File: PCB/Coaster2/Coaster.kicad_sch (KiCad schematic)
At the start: 1028 parts, among them J1 Conn_01x03, J2 Conn_01x03

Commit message: Improved for new KiCAD - needs more work on track nets
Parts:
- removed C212, C213, C214, C215, C216, C217, C218, C219, C220, C221, C222, C223, C224, C225, C226, C227, C228, C229, C230, C231, C232, C233, C234, C235, C236, C237, C238, C239, C240, C241, C242, C243, C244, C245, C246, C247, C248, C249, C250, C251, C252, C253, C254, C255, C256, C257, C258, C259, C260, C261, C262, C263, C264, C265, C266, C267, C268, C269, C270, C271, C272, C273, C274, C275, C276, C277, C278, C279, C280, C281, C282, C283, C284, C285, C286, C287, C288, C289, C290, C291, C292, C293, C294, C295, C296, C297, C298, C299, C300, C301, C302, C303, C304, C305, C306, C307, C308, C309, C310, C311, C312, C313, C314, C315, C316, C317, C318, C319, C320, C321, C322, C323, C324, C325, C326, C327, C328, C329, C330, C331, C332, C333, C334, C335, C336, C337, C338, C339, C340, C341, C342, C343, C344, C345, C346, C347, C348, C349, C350, C351, C352, C353, C354, C355, C356, C357, C358, C359, C360, C361, C362, C363, C364, C365, C366, C367, C368, C369, C370, C371, C372, C373, C374, C375, C376, C377, C378, C379, C380, C381, C382, C383, C384, C385, C386, C387, C388, C389, C390, C391, C392, C393, C394, C395, C396, C397, C398, C399, C400, C401, C402, C403, C404, C405, C406, C407, C408, C409, C410, C411, C412, C413, C414, C415, C416, C417, C418, C419, C420, C421, C422, C423, C424, C425, C426, C427, C428, C429, C430, C431, C432, C433, C434, C435, C436, C437, C438, C439, C440, C441, C442, C443, C444, C445, C446, C447, C448, C449, C450, C451, C452, C453, C454, C455, C456, C457, C458, C459, C460, C461, C462, C463, C464, C465, C466, C467, C468, C469, C470, C471, C472, C473, C474, C475, C476, C477, C478, C479, C480, C481, C482, C483, C484, C485, C486, C487, C488, C489, C490, C491, C492, C493, C494, C495, C496, C497, C498, C499, C500, C501, C502, C503, C504, C505, C506, C507: 100nF, RevK:C_0402, symbol Device:C
- removed D212, D213, D214, D215, D216, D217, D218, D219, D220, D221, D222, D223, D224, D225, D226, D227, D228, D229, D230, D231, D232, D233, D234, D235, D236, D237, D238, D239, D240, D241, D242, D243, D244, D245, D246, D247, D248, D249, D250, D251, D252, D253, D254, D255, D256, D257, D258, D259, D260, D261, D262, D263, D264, D265, D266, D267, D268, D269, D270, D271, D272, D273, D274, D275, D276, D277, D278, D279, D280, D281, D282, D283, D284, D285, D286, D287, D288, D289, D290, D291, D292, D293, D294, D295, D296, D297, D298, D299, D300, D301, D302, D303, D304, D305, D306, D307, D308, D309, D310, D311, D312, D313, D314, D315, D316, D317, D318, D319, D320, D321, D322, D323, D324, D325, D326, D327, D328, D329, D330, D331, D332, D333, D334, D335, D336, D337, D338, D339, D340, D341, D342, D343, D344, D345, D346, D347, D348, D349, D350, D351, D352, D353, D354, D355, D356, D357, D358, D359, D360, D361, D362, D363, D364, D365, D366, D367, D368, D369, D370, D371, D372, D373, D374, D375, D376, D377, D378, D379, D380, D381, D382, D383, D384, D385, D386, D387, D388, D389, D390, D391, D392, D393, D394, D395, D396, D397, D398, D399, D400, D401, D402, D403, D404, D405, D406, D407, D408, D409, D410, D411, D412, D413, D414, D415, D416, D417, D418, D419, D420, D421, D422, D423, D424, D425, D426, D427, D428, D429, D430, D431, D432, D433, D434, D435, D436, D437, D438, D439, D440, D441, D442, D443, D444, D445, D446, D447, D448, D449, D450, D451, D452, D453, D454, D455, D456, D457, D458, D459, D460, D461, D462, D463, D464, D465, D466, D467, D468, D469, D470, D471, D472, D473, D474, D475, D476, D477, D478, D479, D480, D481, D482, D483, D484, D485, D486, D487, D488, D489, D490, D491, D492, D493, D494, D495, D496, D497, D498, D499, D500, D501, D502, D503, D504, D505, D506, D507: XL-1010RGBC-WS2812B, RevK:SMD1010, symbol RevK:WS2812B-1mm
- removed FID5, FID6: Fiducial, RevK:Hole-Tooling, symbol Mechanical:Fiducial
- removed J1, J2: Conn_01x03, RevK:3-PADS, symbol Connector_Generic:Conn_01x03
- removed Z5, Z6: Hidden, RevK:PCB-Join1, symbol RevK:Hidden
- FID4: footprint Fiducial:Fiducial_1mm_Mask2mm -> RevK:Hole-Tooling
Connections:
- net GND: no longer C208.2, C209.2, C210.2, C211.2, D208.3 (-), D209.3 (-), D210.3 (-), D211.3 (-)
- new net: C208.2, C209.2, C210.2, C211.2, D208.3 (-), D209.3 (-), D210.3 (-), D211.3 (-)
- no-connect marks 0 -> 1
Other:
- moved on the sheet: C1, C10, C100, C101, C102, C103, C104, C105, C106, C107, C108, C109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

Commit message: 199 LEDs
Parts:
- removed C200, C201, C202, C203, C204, C205, C206, C207, C208, C209, C210, C211: 100nF, RevK:C_0402, symbol Device:C
- removed D200, D201, D202, D203, D204, D205, D206, D207, D208, D209, D210, D211: XL-1010RGBC-WS2812B, RevK:SMD1010, symbol RevK:WS2812B-1mm
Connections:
- net GND: no longer C198.2, C199.2, D198.3 (-), D199.3 (-)
- new net: C198.2, C199.2, D198.3 (-), D199.3 (-)
- no-connect marks 1 -> 0

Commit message: Connection
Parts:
- added TP1: GND, RevK:Round, symbol Connector:TestPoint
- added TP2: DIN, RevK:Round, symbol Connector:TestPoint
- added TP3: PWR, RevK:Round, symbol Connector:TestPoint
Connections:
- net GND: now also C198.2, C199.2, D198.3 (-), D199.3 (-), TP1.1
- net VCC: now also TP3.1
- net at D1.4 (I): now also TP2.1

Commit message: Tracked
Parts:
- removed C103, C108, C109, C110, C111, C113, C114, C115, C116, C117, C118, C119, C120, C121, C122, C123, C124, C125, C126, C127, C128, C129, C130, C131, C132, C133, C134, C135, C136, C137, C138, C139, C140, C141, C142, C143, C144, C145, C146, C147, C148, C149, C150, C151, C152, C153, C154, C155, C156, C157, C158, C159, C160, C161, C162, C163, C164, C165, C166, C167, C168, C169, C170, C171, C172, C173, C174, C175, C176, C177, C178, C179, C180, C181, C182, C183, C184, C185, C186, C187, C188, C189, C190, C191, C192, C193, C194, C195, C196, C197, C198, C199: 100nF, RevK:C_0402, symbol Device:C
- removed D101, D102, D103, D104, D105, D106, D107, D108, D109, D110, D111, D112, D113, D114, D115, D116, D117, D118, D119, D120, D121, D122, D123, D124, D125, D126, D127, D128, D129, D130, D131, D132, D133, D134, D135, D136, D137, D138, D139, D140, D141, D142, D143, D144, D145, D146, D147, D148, D149, D150, D151, D152, D153, D154, D155, D156, D157, D158, D159, D160, D161, D162, D163, D164, D165, D166, D167, D168, D169, D170, D171, D172, D173, D174, D175, D176, D177, D178, D179, D180, D181, D182, D183, D184, D185, D186, D187, D188, D189, D190, D191, D192, D193, D194, D195, D196, D197, D198, D199: XL-1010RGBC-WS2812B, RevK:SMD1010, symbol RevK:WS2812B-1mm
- removed TP1: GND, RevK:Round, symbol Connector:TestPoint
- removed TP2: DIN, RevK:Round, symbol Connector:TestPoint
- removed TP3: PWR, RevK:Round, symbol Connector:TestPoint
- removed Z1, Z2, Z3, Z4: Hidden, RevK:PCB-Join1, symbol RevK:Hidden
- added C103: 220uF Tant, RevK:CP_EIA-3528-21_Kemet-B, symbol Device:C_Polarized
- added C109: 10uF 35V, RevK:C_0603_, symbol RevK:Hidden
- added C110: 10uF 6.3V, RevK:C_0603_, symbol RevK:Hidden
- added C111: 100nF, RevK:C_0603_, symbol RevK:Hidden
- added FID5: Fiducial, RevK:Hole-Tooling, symbol Mechanical:Fiducial
- added FID6: Fiducial, Fiducial:Fiducial_1mm_Mask2mm, symbol Mechanical:Fiducial
- added J1: Reset, RevK:AA-Pad, symbol Connector_Generic:Conn_01x02
- added J3: USB-C-Socket-H, RevK:USB-C-Socket-H, symbol RevK:USB-C-Socket-H
- added J4: TC2030-USB-NL-DS, RevK:Tag-Connect_TC2030-IDC-NL_2x03_P1.27mm_Vertical, symbol RevK:TC2030-USB-NL
- added L1: 10uH, RevK:L_4x4_, symbol RevK:Hidden
- added R1: 10K, RevK:R_0402, symbol Device:R
- added R4: 124k, RevK:R_0402_, symbol RevK:Hidden
- added R5: 39k2, RevK:R_0402_, symbol RevK:Hidden
- added R6: 1M, RevK:R_0402_, symbol RevK:Hidden
- added R7, R8: 5K1, RevK:R_0402, symbol Device:R
- added U1: ESP32-S3-MINI-1, RevK:ESP32-S3-MINI-1, symbol RevK:ESP32-S3-MINI-1-N4R2
- added U2: MD8942, RevK:SOT-23-6-MD8942, symbol RevK:MD89420-RegBlock
- added U3: ICS43434_MEMS_Mic, RevK:ICS43434_MEMS_Mic, symbol RevK:ICS43434_MEMS_Mic
- C102: value 100nF -> 22uF; footprint RevK:C_0402 -> RevK:C_0603
- C104, C105, C107: value 100nF -> 10uF 35V; footprint RevK:C_0402 -> RevK:C_0603; LCSC Part # (none) -> C194427
- C106: value 100nF -> 1uF
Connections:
- net GND: now also C112.1, C103.2, J1.1 (Pin_1), J3.A1 (GND), J3.A12 (GND), J3.B1 (GND), J3.B12 (GND), J3.S1 (SHIELD), J4.5 (GND), J4.6 (GND), R7.2, R8.1, U1.1 (GND), U1.2 (GND), U1.42 (GND), U1.43 (GND), U1.46 (GND), U1.47 (GND), U1.48 (GND), U1.49 (GND), U1.50 (GND), U1.51 (GND), U1.52 (GND), U1.53 (GND), U1.54 (GND), U1.55 (GND), U1.56 (GND), U1.57 (GND), U1.58 (GND), U1.59 (GND), U1.60 (GND), U1.61 (GND), U1.62 (GND), U1.63 (GND), U1.64 (GND), U1.65 (GND), U2.2 (GND), U2.7 (GND), U3.2 (LR), U3.3 (GND); no longer C112.2
- net LED: now reaches D1.4 (I)
- net LED: now also U1.33 (GPIO37)
- net VCC renamed VBUS
- net VBUS: now also J3.A4 (VBUS), J3.A9 (VBUS), J3.B4 (VBUS), J3.B9 (VBUS), J4.1 (VBUS), J4.2 (VBUS), U2.5 (VIN); no longer C101.1, C102.1, C106.1, C107.1, C112.1
- new net: J3.A5 (CC1), R7.1
- new net: C106.1, R1.2, U1.45 (EN)
- new net: J3.B5 (CC2), R8.2
- new net: J1.2 (Pin_2), U1.25 (GPIO21)
- new net +3V3: C101.1, C102.1, C103.1, C107.1, C112.2, R1.1, U1.3 (3V3), U2.8 (VOUT), U3.5 (VDD)
- new net D+: J3.A6 (D+), J3.B6 (D+), J4.4 (D+), U1.24 (GPIO20)
- new net D-: J3.A7 (D-), J3.B7 (D-), J4.3 (D-), U1.23 (GPIO19)
- new net SCK: U1.38 (GPIO42), U3.4 (SCK)
- new net SD: U1.37 (GPIO41), U3.6 (SD)
- new net WS: U1.36 (GPIO40), U3.1 (WS)
- no-connect marks 0 -> 33

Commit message: 124 LEDs
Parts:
- removed J1: Reset, RevK:AA-Pad, symbol Connector_Generic:Conn_01x02
- added C101, C102, C103, C104, C105, C106, C107, C108, C109, C110, C111, C112, C113, C114, C115, C116, C117, C118, C119, C120, C121, C122, C123, C124: 100nF, RevK:C_0402, symbol Device:C
- added D101, D102, D103, D104, D105, D106, D107, D108, D109, D110, D111, D112, D113, D114, D115, D116, D117, D118, D119, D120, D121, D122, D123, D124: XL-1010RGBC-WS2812B, RevK:SMD1010, symbol RevK:WS2812B-1mm
- renumbered C101 to C129, C102 to C130, C103 to C131, C112 to C132, C104 to C133, C106 to C134, C105 to C135, C107 to C136, C109 to C137, C110 to C138, C111 to C139, FID5 to FID1, FID4 to FID3, FID6 to FID4, FID1 to FID5, FID3 to FID6, J4 to J2, R4 to R2, R5 to R3, R6 to R4, R7 to R5, R8 to R6, U3 to U1, U1 to U2, U2 to U3
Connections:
- net GND: now also C101.2, C102.2, C103.2, C104.2, C105.2, C106.2, C107.2, C108.2, C109.2, C110.2, C111.2, C112.2, C113.2, C114.2, C115.2, C116.2, C117.2, C118.2, C119.2, C120.2, C121.2, C122.2, C123.2, C124.2, D101.3 (-), D102.3 (-), D103.3 (-), D104.3 (-), D105.3 (-), D106.3 (-), D107.3 (-), D108.3 (-), D109.3 (-), D110.3 (-), D111.3 (-), D112.3 (-), D113.3 (-), D114.3 (-), D115.3 (-), D116.3 (-), D117.3 (-), D118.3 (-), D119.3 (-), D120.3 (-), D121.3 (-), D122.3 (-), D123.3 (-), D124.3 (-)
- net VBUS: now also C101.1, C102.1, C103.1, C104.1, C105.1, C106.1, C107.1, C108.1, C109.1, C110.1, C111.1, C112.1, C113.1, C114.1, C115.1, C116.1, C117.1, C118.1, C119.1, C120.1, C121.1, C122.1, C123.1, C124.1, D101.2 (+), D102.2 (+), D103.2 (+), D104.2 (+), D105.2 (+), D106.2 (+), D107.2 (+), D108.2 (+), D109.2 (+), D110.2 (+), D111.2 (+), D112.2 (+), D113.2 (+), D114.2 (+), D115.2 (+), D116.2 (+), D117.2 (+), D118.2 (+), D119.2 (+), D120.2 (+), D121.2 (+), D122.2 (+), D123.2 (+), D124.2 (+)
- net at D100.1 (O): now also D101.4 (I)
- new net: D117.1 (O), D118.4 (I)
- new net: D116.1 (O), D117.4 (I)
- new net: D109.1 (O), D110.4 (I)
- new net: D108.1 (O), D109.4 (I)
- new net: D115.1 (O), D116.4 (I)
- new net: D121.1 (O), D122.4 (I)
- new net: D120.1 (O), D121.4 (I)
- new net: D113.1 (O), D114.4 (I)
- new net: D112.1 (O), D113.4 (I)
- new net: D104.1 (O), D105.4 (I)
- new net: D103.1 (O), D104.4 (I)
- new net: D107.1 (O), D108.4 (I)
- new net: D102.1 (O), D103.4 (I)
- new net: D110.1 (O), D111.4 (I)
- new net: D114.1 (O), D115.4 (I)
- new net: D123.1 (O), D124.4 (I)
- new net: D101.1 (O), D102.4 (I)
- new net: D111.1 (O), D112.4 (I)
- new net: D119.1 (O), D120.4 (I)
- new net: D118.1 (O), D119.4 (I)
- new net: D122.1 (O), D123.4 (I)
- new net: D106.1 (O), D107.4 (I)
- new net: D105.1 (O), D106.4 (I)
- no-connect marks 33 -> 32
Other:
- moved on the sheet: C129, C130, C131, C132, C133, C134, C135, C136, C137, C138, C139, J2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

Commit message: SS
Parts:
- added J1: Reset, RevK:AA-Pad, symbol Connector_Generic:Conn_01x02
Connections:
- net GND: now also J1.1 (Pin_1)
- net at U2.25 (GPIO21): now also J1.2 (Pin_2)
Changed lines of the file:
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@@
+	)
+	(symbol
+		(lib_id "Connector_Generic:Conn_01x02")
+		(at 170.18 83.82 180)
+		(unit 1)
+		(exclude_from_sim no)
+		(in_bom no)
+		(on_board yes)
+		(dnp no)
+		(fields_autoplaced yes)
+		(property "Reference" "J1"
+			(at 170.18 75.8655 0)
+			(effects
+				(font
+					(size 1.27 1.27)
+				)
+			)
+		)
+		(property "Value" "Reset"
+			(at 170.18 78.2898 0)
+			(effects
+				(font
+					(size 1.27 1.27)
+				)
+			)
+		)
+		(property "Footprint" "RevK:AA-Pad"
+			(at 170.18 83.82 0)
+			(effects
+				(font
+					(size 1.27 1.27)
+				)
+				(hide yes)
+			)
+		)
+		(property "Datasheet" "~"
+			(at 170.18 83.82 0)
+			(effects
+				(font
+					(size 1.27 1.27)
+				)
+				(hide yes)
+			)
+		)
+		(property "Description" "Generic connector, single row, 01x02, script generated (kicad-library-utils/schlib/autogen/connector/)"
+			(at 170.18 83.82 0)
+			(effects
+				(font
+					(size 1.27 1.27)
+				)
+				(hide yes)
+			)
+		)
+		(pin "2"
+		)
+		(pin "1"
+		)
+		(instances
+			(project "Coaster"
+				(path "/46c350bb-7de4-4e81-aafd-4af55e37aab0"
+					(reference "J1")
+					(unit 1)
+				)
+			)
+		)
 	)
 	(symbol

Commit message: Final, and spacers
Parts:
- removed FID1, FID2, FID3: Fiducial, RevK:Hole-Tooling, symbol Mechanical:Fiducial
- removed FID4, FID5, FID6: Fiducial, Fiducial:Fiducial_1mm_Mask2mm, symbol Mechanical:Fiducial
- added PCB1: 120x120, RevK:PCB120120, symbol RevK:PCB
- added V1, V2, V3, V4: ~, RevK:VCUT120N, symbol RevK:VCUT

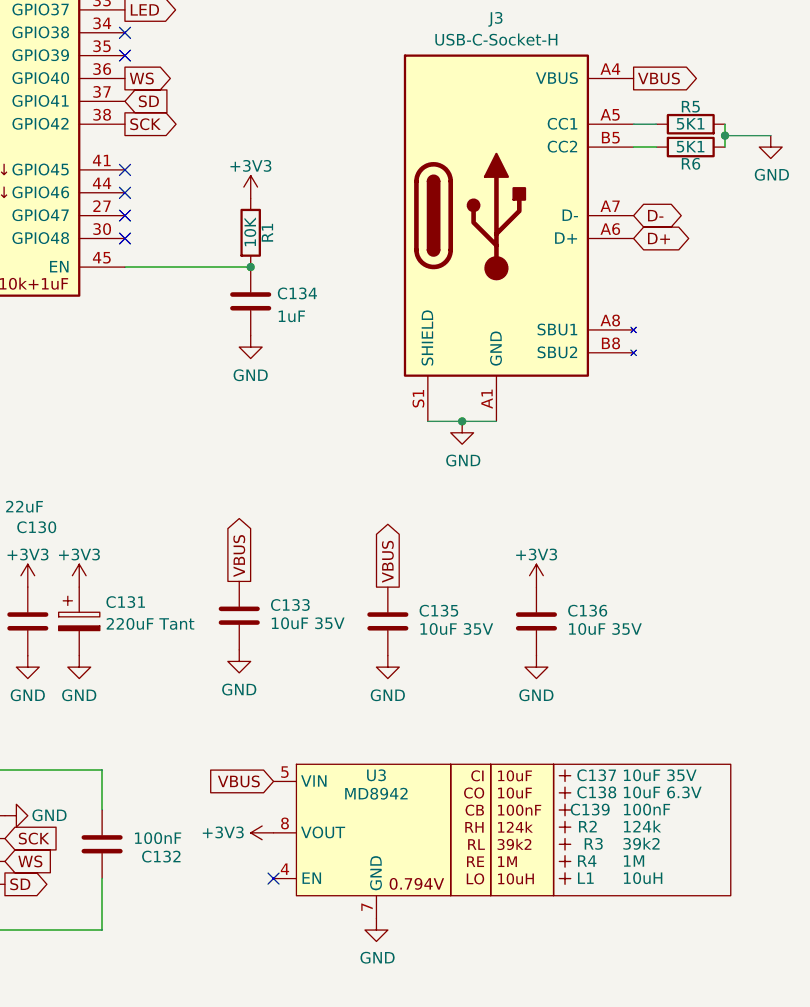
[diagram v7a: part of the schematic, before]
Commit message: LED35 added
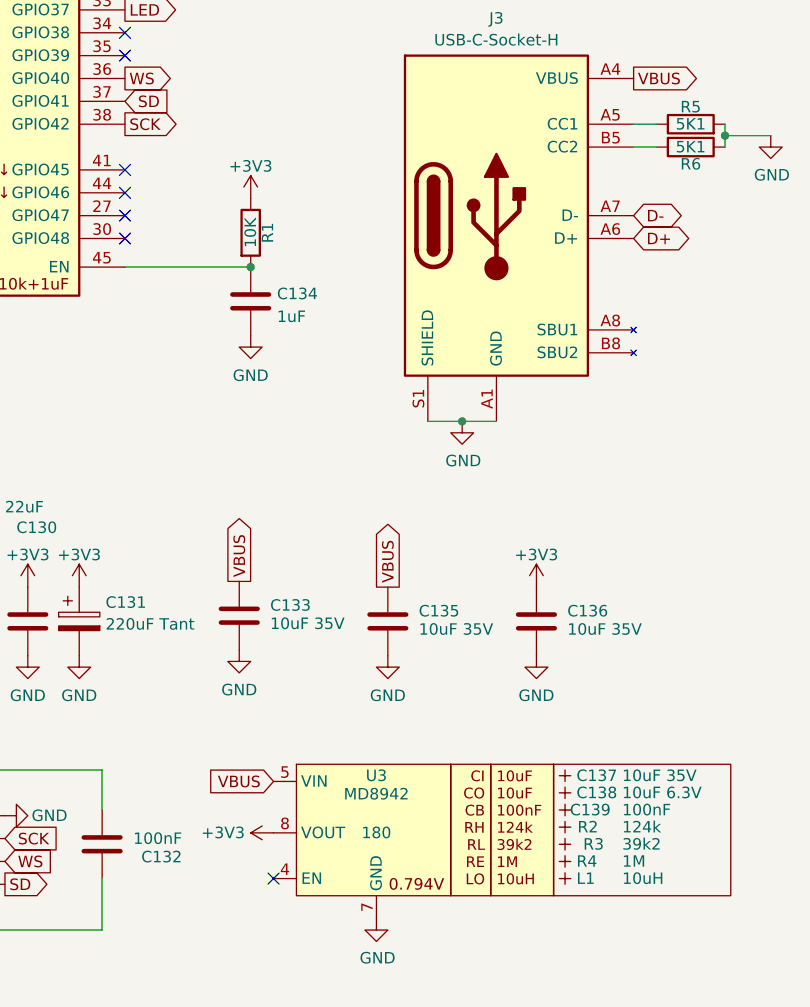
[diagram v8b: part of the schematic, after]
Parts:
- U3: Rotation Offset (none) -> 180
